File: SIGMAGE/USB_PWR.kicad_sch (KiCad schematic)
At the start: 44 parts, among them J1 UJ31CHG2SMTTR, U1 MAX8902BATA/V+T, U2 MAX8902BATA/V+T, U3 MAX8902BATA/V+T

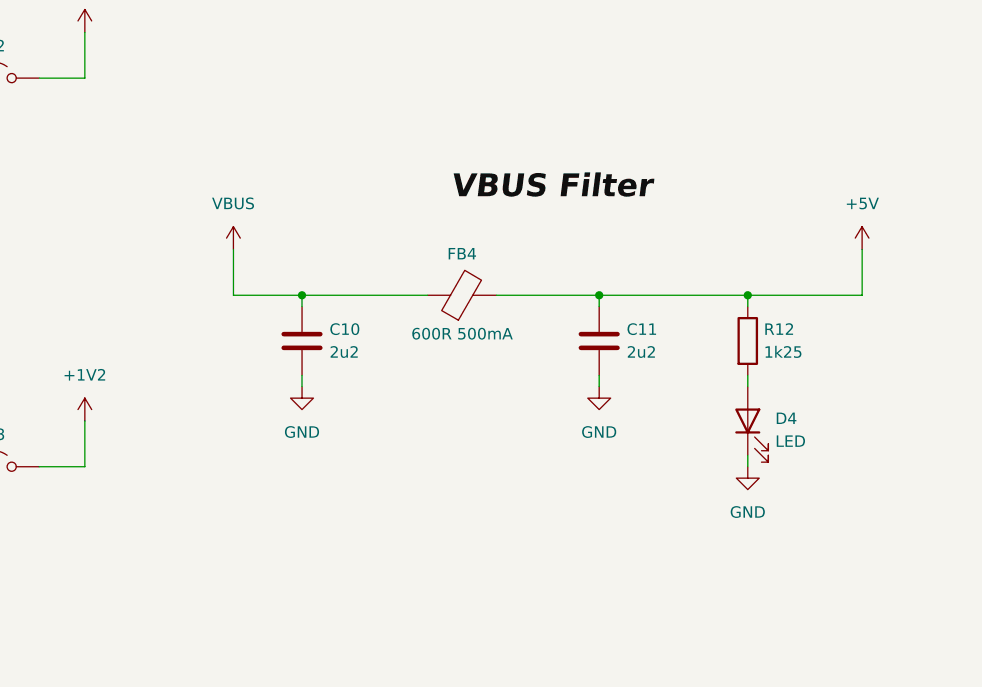
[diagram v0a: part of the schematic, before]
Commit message: Added RJ45/PHY and MCU
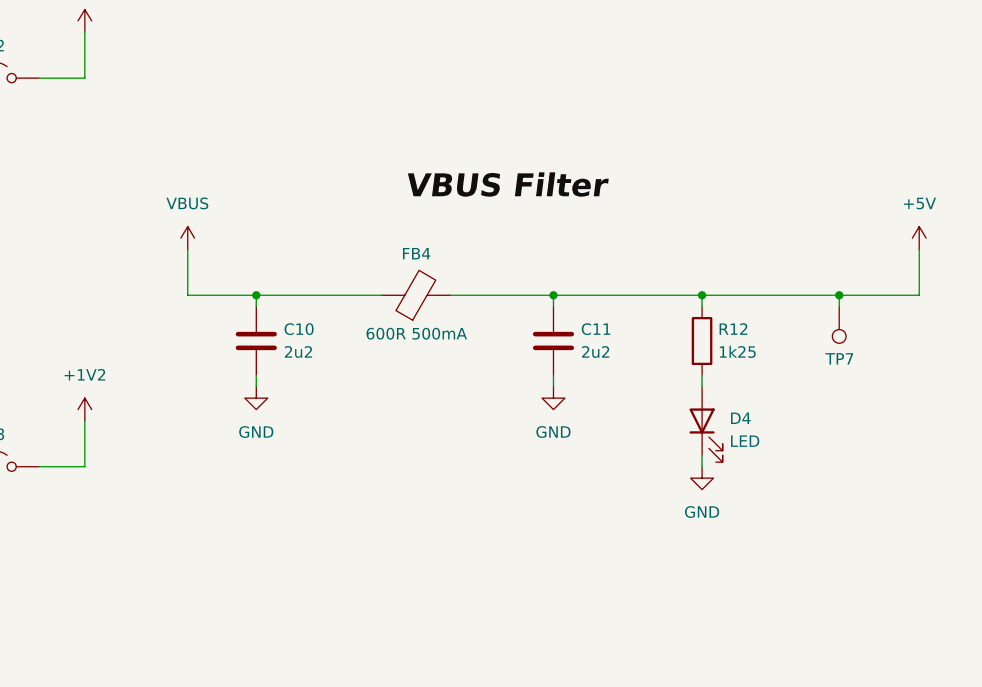
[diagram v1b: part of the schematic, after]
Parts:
- added TP7: 3V3, symbol Connector:TestPoint
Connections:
- net +5V: now also TP7.1
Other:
- moved on the sheet: C10, C11, D4, FB4, R12

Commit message: Finished schematic
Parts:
- added J14, J15, J16, J17: HTSW10807GD, SIGMAGE:HTSW10807GD, symbol SIGMAGE:HTSW10807GD
- added TP8: 3V3, symbol Connector:TestPoint
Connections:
- net +1V2: now also J16.1, J16.10, J16.11, J16.12, J16.13, J16.14, J16.15, J16.16, J16.2, J16.3, J16.4, J16.5, J16.6, J16.7, J16.8, J16.9
- net +2V5: now also J15.1, J15.10, J15.11, J15.12, J15.13, J15.14, J15.15, J15.16, J15.2, J15.3, J15.4, J15.5, J15.6, J15.7, J15.8, J15.9
- net +3V3: now also J14.1, J14.10, J14.11, J14.12, J14.13, J14.14, J14.15, J14.16, J14.2, J14.3, J14.4, J14.5, J14.6, J14.7, J14.8, J14.9
- net +5V: now also TP8.1; no longer TP7.1
- net GND: now also J17.1, J17.10, J17.11, J17.12, J17.13, J17.14, J17.15, J17.16, J17.2, J17.3, J17.4, J17.5, J17.6, J17.7, J17.8, J17.9
- net VBUS: now also TP7.1
- no-connect marks 13 -> 17
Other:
- moved on the sheet: C1, C10, C11, C2, C3, C4, C5, C6, C7, C8, C9, D1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

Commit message: Added PCB layout and started routing
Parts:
- removed TP1, TP2, TP3, TP4, TP5, TP6, TP7, TP8: 3V3, symbol Connector:TestPoint
- C1, C10, C11, C2, C3, C4, C5, C6, C7, C8, C9, FB1, FB2, FB3, FB4: footprint (none) -> Capacitor_SMD:C_0603_1608Metric
- D1, D2, D3, D4: footprint (none) -> LED_SMD:LED_0603_1608Metric
- JP1, JP2, JP3: footprint (none) -> TestPoint:TestPoint_Bridge_Pitch2.54mm_Drill0.7mm
- R1, R10, R11, R12, R2, R3, R4, R5, R6, R7, R8, R9: footprint (none) -> Resistor_SMD:R_0603_1608Metric
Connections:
- net +1V2: now also FB3.2, JP3.1 (A)
- net +2V5: now also FB2.2, JP2.1 (A)
- net +3V3: now also FB1.2, JP1.1 (A)
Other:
- moved on the sheet: C1, C2, C3, C4, C5, C6, C7, C8, C9, D1, D2, D3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

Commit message: Finished PCB
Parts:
- removed JP1, JP2, JP3: Jumper_2_Open, TestPoint:TestPoint_Bridge_Pitch2.54mm_Drill0.7mm, symbol Jumper:Jumper_2_Open
- added JP1, JP2, JP3: Jumper_2_Bridged, Panelization:MouseBite-Slot-Jumper_0201, symbol Jumper:Jumper_2_Bridged
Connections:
- net +1V2: now also JP3.2 (B); no longer FB3.2
- net +2V5: now also JP2.2 (B); no longer FB2.2
- net +3V3: now also JP1.2 (B); no longer FB1.2
- new net: FB3.2, JP3.1 (A)
- new net: FB1.2, JP1.1 (A)
- new net: FB2.2, JP2.1 (A)

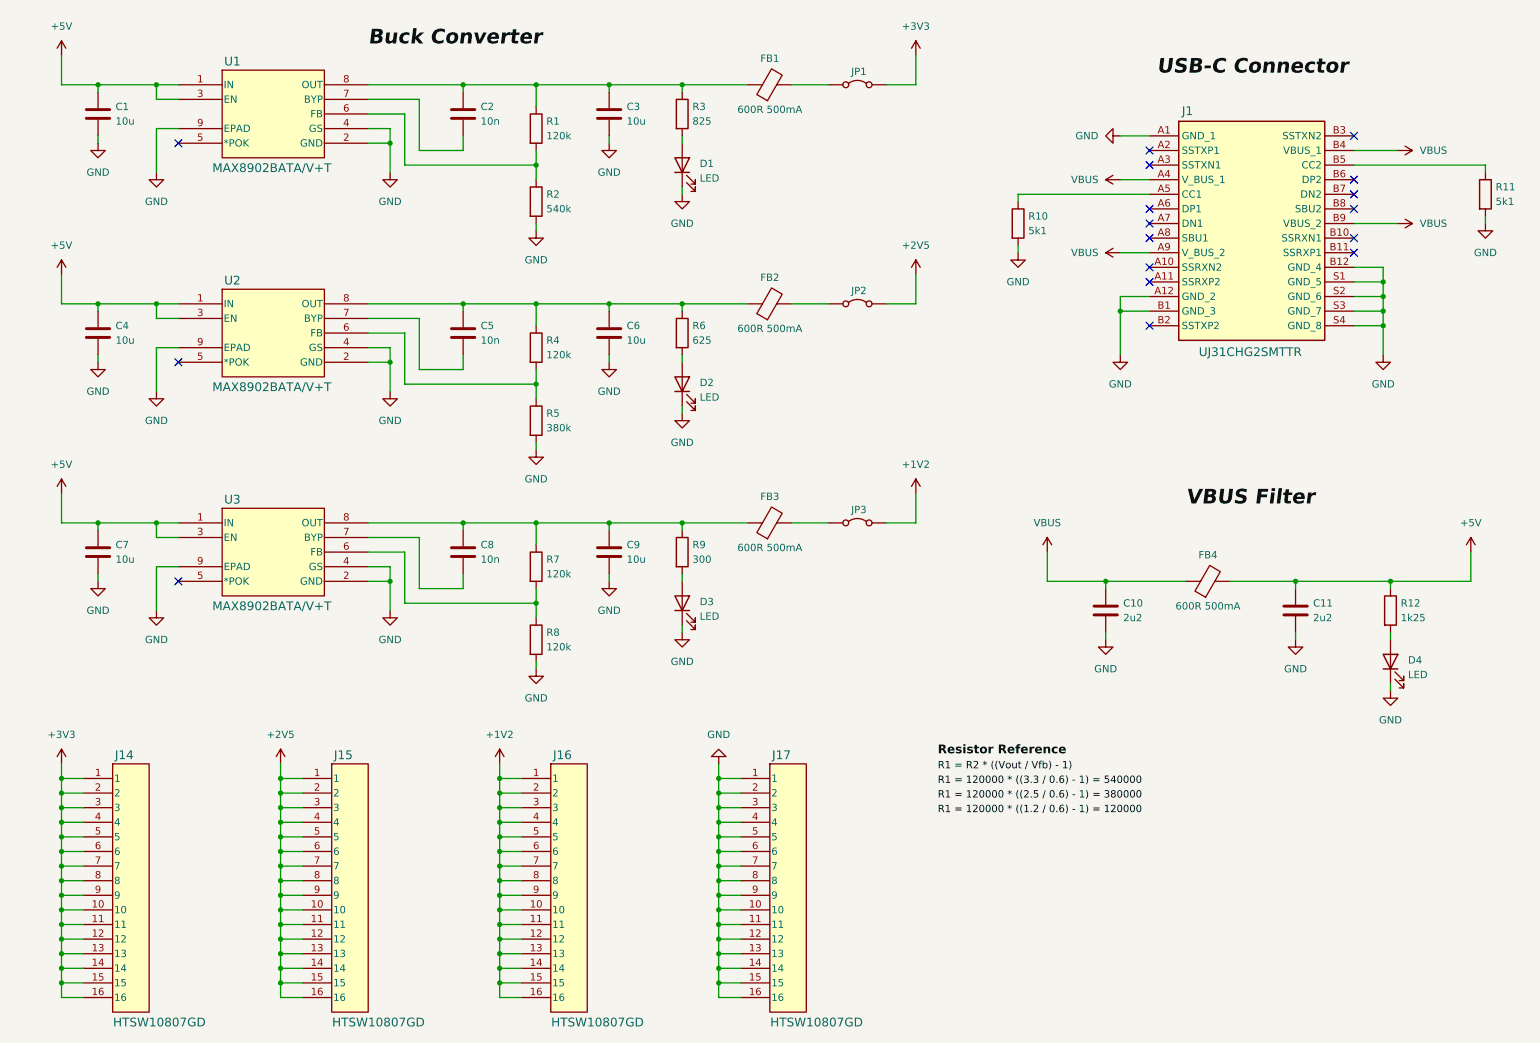
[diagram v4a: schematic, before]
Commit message: Final touches, PCB layout is still horrible, will fix in MK II
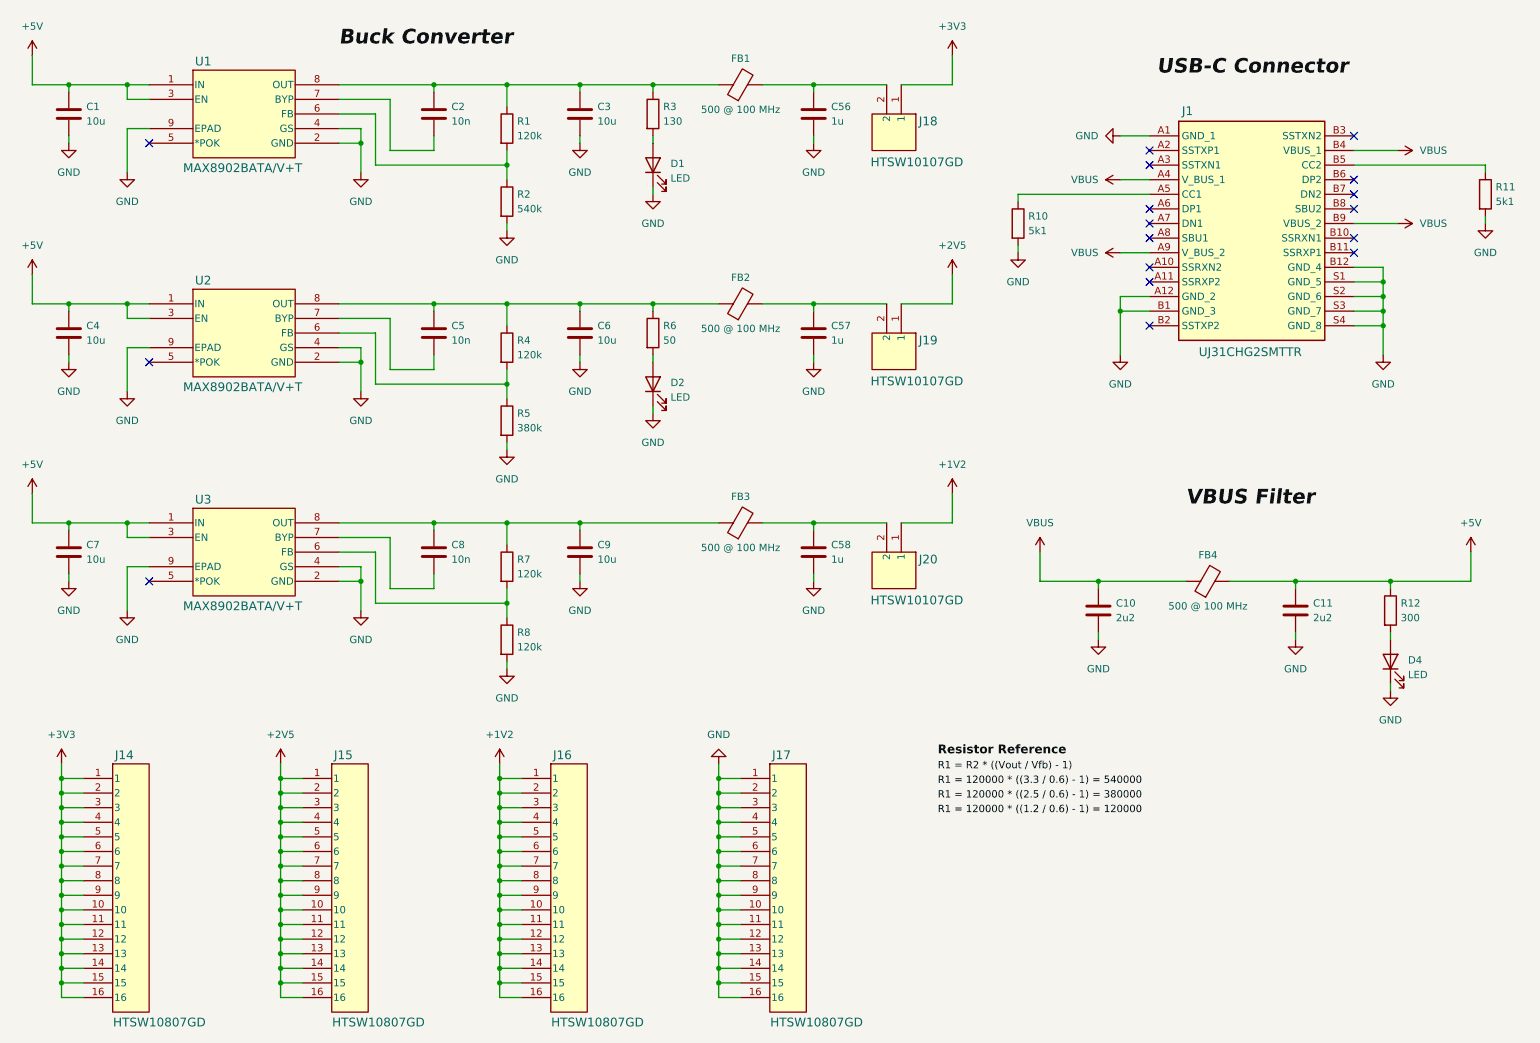
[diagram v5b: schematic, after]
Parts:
- removed D3: LED, LED_SMD:LED_0603_1608Metric, symbol Device:LED
- removed JP1, JP2, JP3: Jumper_2_Bridged, Panelization:MouseBite-Slot-Jumper_0201, symbol Jumper:Jumper_2_Bridged
- removed R9: 300, Resistor_SMD:R_0603_1608Metric, symbol Device:R
- added C56, C57, C58: 1u, Capacitor_SMD:C_0603_1608Metric, symbol Device:C
- added J18, J19, J20: HTSW10107GD, SIGMAGE:HTSW10107GD, symbol SIGMAGE:HTSW10107GD
- FB1, FB2, FB3, FB4: value 600R 500mA -> 500 @ 100 MHz
- R12: value 1k25 -> 300
- R3: value 825 -> 130
- R6: value 625 -> 50
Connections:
- net +1V2: now also J20.1
- net +2V5: now also J19.1
- net +3V3: now also J18.1
- net GND: now also C56.2, C57.2, C58.2
- net at FB3.2: now also C58.1, J20.2
- net at FB1.2: now also C56.1, J18.2
- net at FB2.2: now also C57.1, J19.2
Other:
- moved on the sheet: C1, C10, C2, C3, C4, C5, C6, C7, C8, C9, D1, D2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

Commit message: Again some touches against DigiKey's assortment
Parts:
- added R32: 200k, Resistor_SMD:R_0603_1608Metric, symbol Device:R
- added R9: 270k, Resistor_SMD:R_0603_1608Metric, symbol Device:R
- R2: value 540k -> 270k
- R5: value 380k -> 180k
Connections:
- net GND: now also R32.2, R9.2; no longer R2.2, R5.2
- new net: R32.1, R5.2
- new net: R2.2, R9.1
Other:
- moved on the sheet: R2, R5
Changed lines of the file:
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@@
 	(wire
 		(pts
-			(xy 102.87 81.28) (xy 102.87 83.82)
-		)
-		(stroke
-			(width 0)
-			(type default)
-		)
-	)
-	(wire
-		(pts
 			(xy 139.7 157.48) (xy 143.51 157.48)
 		)
@@
 	(wire
 		(pts
-			(xy 102.87 53.34) (xy 102.87 54.61)
-		)
-		(stroke
-			(width 0)
-			(type default)
-		)
-	)
-	(wire
-		(pts
 			(xy 63.5 154.94) (xy 67.31 154.94)
 		)
@@
 	(wire
 		(pts
-			(xy 102.87 91.44) (xy 102.87 92.71)
-		)
-		(stroke
-			(width 0)
-			(type default)
-		)
-	)
-	(wire
-		(pts
 			(xy 139.7 154.94) (xy 143.51 154.94)
 		)
@@
 	(wire
 		(pts
+			(xy 102.87 82.55) (xy 102.87 81.28)
+		)
+		(stroke
+			(width 0)
+			(type default)
+		)
+	)
+	(wire
+		(pts
 			(xy 25.4 180.34) (xy 25.4 177.8)
 		)
@@
 	(wire
 		(pts
-			(xy 102.87 43.18) (xy 102.87 45.72)
+			(xy 102.87 29.21) (xy 102.87 33.02)
 		)
 		(stroke
@@
 	(wire
 		(pts
-			(xy 102.87 29.21) (xy 102.87 33.02)
+			(xy 73.66 29.21) (xy 90.17 29.21)
 		)
 		(stroke
@@
 	(wire
 		(pts
-			(xy 73.66 29.21) (xy 90.17 29.21)
+			(xy 26.67 105.41) (xy 26.67 106.68)
 		)
 		(stroke
@@
 	(wire
 		(pts
-			(xy 26.67 105.41) (xy 26.67 106.68)
+			(xy 80.01 119.38) (xy 102.87 119.38)
 		)
 		(stroke
@@
 	(wire
 		(pts
-			(xy 80.01 119.38) (xy 102.87 119.38)
+			(xy 63.5 187.96) (xy 63.5 185.42)
 		)
 		(stroke
@@
 	(wire
 		(pts
-			(xy 63.5 187.96) (xy 63.5 185.42)
+			(xy 26.67 29.21) (xy 26.67 30.48)
 		)
 		(stroke
@@
 	(wire
 		(pts
-			(xy 26.67 29.21) (xy 26.67 30.48)
+			(xy 90.17 67.31) (xy 90.17 68.58)
 		)
 		(stroke
@@
 	(wire
 		(pts
-			(xy 90.17 67.31) (xy 90.17 68.58)
+			(xy 102.87 44.45) (xy 102.87 43.18)
 		)
 		(stroke
@@
 	(symbol
 		(lib_id "power:GND")
-		(at 102.87 92.71 0)
+		(at 102.87 97.79 0)
 		(unit 1)
 		(exclude_from_sim no)
@@
 		(dnp no)
 		(property "Reference" "#PWR013"
-			(at 102.87 99.06 0)
+			(at 102.87 104.14 0)
 			(effects
 				(font
@@
 		)
 		(property "Value" "GND"
-			(at 102.87 97.79 0)
+			(at 102.87 102.87 0)
 			(effects
 				(font
@@
 		)
 		(property "Footprint" ""
-			(at 102.87 92.71 0)
+			(at 102.87 97.79 0)
 			(effects
 				(font
@@
 		)
 		(property "Datasheet" ""
-			(at 102.87 92.71 0)
+			(at 102.87 97.79 0)
 			(effects
 				(font
@@
 		)
 		(property "Description" "Power symbol creates a global label with name \"GND\" , ground"
-			(at 102.87 92.71 0)
+			(at 102.87 97.79 0)
 			(effects
 				(font
@@
 	)
 	(symbol
+		(lib_id "Device:R")
+		(at 102.87 93.98 0)
+		(unit 1)
+		(exclude_from_sim no)
+		(in_bom yes)
+		(on_board yes)
+		(dnp no)
+		(property "Reference" "R32"
+			(at 104.648 92.71 0)
+			(effects
+				(font
+					(size 1.27 1.27)
+				)
+				(justify left)
+			)
+		)
+		(property "Value" "200k"
+			(at 104.648 95.25 0)
+			(effects
+				(font
+					(size 1.27 1.27)
+				)
+				(justify left)
+			)
+		)
+		(property "Footprint" "Resistor_SMD:R_0603_1608Metric"
+			(at 101.092 93.98 90)
+			(effects
+				(font
+					(size 1.27 1.27)
+				)
+				(hide yes)
+			)
+		)
+		(property "Datasheet" "~"
+			(at 102.87 93.98 0)
+			(effects
+				(font
+					(size 1.27 1.27)
+				)
+				(hide yes)
+			)
+		)
+		(property "Description" "Resistor"
+			(at 102.87 93.98 0)
+			(effects
+				(font
+					(size 1.27 1.27)
+				)
+				(hide yes)
+			)
+		)
+		(pin "2"
+		)
+		(pin "1"
+		)
+		(instances
+			(project "SIGMAGE"
+				(path "/6fbe3371-b6a3-4e28-aef4-4e5865f4674e/235daf91-2b59-4415-8b4f-a5ae9861f33b"
+					(reference "R32")
+					(unit 1)
+				)
+			)
+		)
+	)
+	(symbol
 		(lib_id "Device:LED")
 		(at 128.27 81.28 90)
@@
 	(symbol
 		(lib_id "Device:R")
-		(at 102.87 87.63 0)
+		(at 102.87 86.36 0)
 		(unit 1)
 		(exclude_from_sim no)
@@
 		(dnp no)
 		(property "Reference" "R5"
-			(at 104.648 86.36 0)
+			(at 104.648 85.09 0)
 			(effects
 				(font
@@
 			)
 		)
-		(property "Value" "380k"
-			(at 104.648 88.9 0)
+		(property "Value" "180k"
+			(at 104.648 87.63 0)
 			(effects
 				(font
@@
 		)
 		(property "Footprint" "Resistor_SMD:R_0603_1608Metric"
-			(at 101.092 87.63 90)
+			(at 101.092 86.36 90)
 			(effects
 				(font
@@
 		)
 		(property "Datasheet" "~"
-			(at 102.87 87.63 0)
+			(at 102.87 86.36 0)
 			(effects
 				(font
@@
 		)
 		(property "Description" "Resistor"
-			(at 102.87 87.63 0)
+			(at 102.87 86.36 0)
 			(effects
 				(font
@@
 	(symbol
 		(lib_id "Device:R")
-		(at 102.87 49.53 0)
+		(at 102.87 48.26 0)
 		(unit 1)
 		(exclude_from_sim no)
@@
 		(dnp no)
 		(property "Reference" "R2"
-			(at 104.648 48.26 0)
+			(at 104.648 46.99 0)
 			(effects
 				(font
@@
 			)
 		)
-		(property "Value" "540k"
-			(at 104.648 50.8 0)
+		(property "Value" "270k"
+			(at 104.648 49.53 0)
 			(effects
 				(font
@@
 		)
 		(property "Footprint" "Resistor_SMD:R_0603_1608Metric"
-			(at 101.092 49.53 90)
+			(at 101.092 48.26 90)
 			(effects
 				(font
@@
 		)
 		(property "Datasheet" "~"
-			(at 102.87 49.53 0)
+			(at 102.87 48.26 0)
 			(effects
 				(font
@@
 		)
 		(property "Description" "Resistor"
-			(at 102.87 49.53 0)
+			(at 102.87 48.26 0)
 			(effects
 				(font
@@
 	)
 	(symbol
+		(lib_id "Device:R")
+		(at 102.87 55.88 0)
+		(unit 1)
+		(exclude_from_sim no)
+		(in_bom yes)
+		(on_board yes)
+		(dnp no)
+		(property "Reference" "R9"
+			(at 104.648 54.61 0)
+			(effects
+				(font
+					(size 1.27 1.27)
+				)
+				(justify left)
+			)
+		)
+		(property "Value" "270k"
+			(at 104.648 57.15 0)
+			(effects
+				(font
+					(size 1.27 1.27)
+				)
+				(justify left)
+			)
+		)
+		(property "Footprint" "Resistor_SMD:R_0603_1608Metric"
+			(at 101.092 55.88 90)
+			(effects
+				(font
+					(size 1.27 1.27)
+				)
+				(hide yes)
+			)
+		)
+		(property "Datasheet" "~"
+			(at 102.87 55.88 0)
+			(effects
+				(font
+					(size 1.27 1.27)
+				)
+				(hide yes)
+			)
+		)
+		(property "Description" "Resistor"
+			(at 102.87 55.88 0)
+			(effects
+				(font
+					(size 1.27 1.27)
+				)
+				(hide yes)
+			)
+		)
+		(pin "2"
+		)
+		(pin "1"
+		)
+		(instances
+			(project "SIGMAGE"
+				(path "/6fbe3371-b6a3-4e28-aef4-4e5865f4674e/235daf91-2b59-4415-8b4f-a5ae9861f33b"
+					(reference "R9")
+					(unit 1)
+				)
+			)
+		)
+	)
+	(symbol
 		(lib_id "power:GND")
-		(at 102.87 54.61 0)
+		(at 102.87 59.69 0)
 		(unit 1)
 		(exclude_from_sim no)
@@
 		(fields_autoplaced yes)
 		(property "Reference" "#PWR05"
-			(at 102.87 60.96 0)
+			(at 102.87 66.04 0)
 			(effects
 				(font
@@
 		)
 		(property "Value" "GND"
-			(at 102.87 59.69 0)
+			(at 102.87 64.77 0)
 			(effects
 				(font
@@
 		)
 		(property "Footprint" ""
-			(at 102.87 54.61 0)
+			(at 102.87 59.69 0)
 			(effects
 				(font
@@
 		)
 		(property "Datasheet" ""
-			(at 102.87 54.61 0)
+			(at 102.87 59.69 0)
 			(effects
 				(font
@@
 		)
 		(property "Description" "Power symbol creates a global label with name \"GND\" , ground"
-			(at 102.87 54.61 0)
+			(at 102.87 59.69 0)
 			(effects
 				(font
